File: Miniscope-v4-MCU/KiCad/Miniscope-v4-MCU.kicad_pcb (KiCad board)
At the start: 4 copper layers, 7 x 8 mm, 11 parts, among them J1 Conn_01x14, J2 Conn_01x01, J3 Conn_01x01, J4 Conn_01x01, J5 Conn_01x01, J6 Conn_01x01, J7 Conn_01x01, J8 Conn_01x05, U1 ATmega328-MU

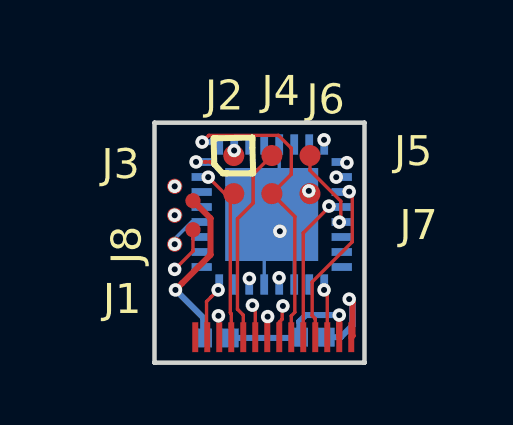
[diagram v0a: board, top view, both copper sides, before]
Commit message: Update MCU PCB with 2x7 grid of FlexPC solder pads
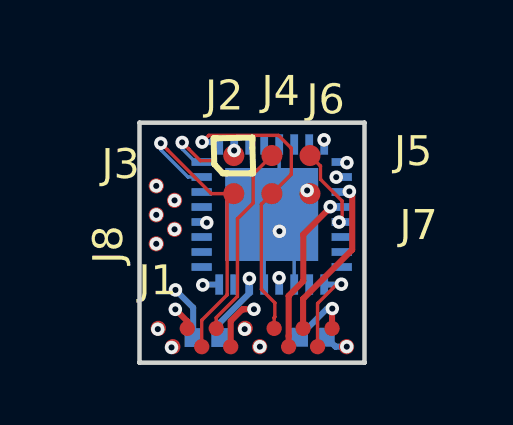
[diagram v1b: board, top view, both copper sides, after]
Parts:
- J1: footprint .Connector:B2B_Flex_14_Single_Row_200x1000_Pad_400P -> .Connector:B2B_Flex_14_Dual_Row_38milx24mil_Pad_20mil
- moved J1 1.27 mm to (50.1, 56.9)
- moved J8 0.61 mm to (50.1, 54.0)
- moved C1 0.34 mm to (51.7, 57.2)
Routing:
- net GND: track 24.3 -> 10.2 mm, vias 4 -> 5
- net +3V3: track 6.00 -> 0.80 mm
- net /MOSI: track 6.33 -> 10.9 mm
- net /MISO: track 8.69 -> 10.4 mm
- net /SCL: track 12.8 -> 11.2 mm
- net /SS_N: track 1.62 -> 3.08 mm
- net /LED: track 1.75 -> 3.07 mm, vias 1 -> 2
- net /MONITOR0: track 7.53 -> 8.39 mm
- net +1V8: track 13.2 -> 12.4 mm
- net /ENT1: track 1.31 -> 1.98 mm, vias 1 -> 2
- net /RESET_N: track 6.19 -> 6.70 mm
- net +5V: vias 0 -> 1
- added copper zone on In4.Cu, net +3V3
- added copper zone on In1.Cu, net GND
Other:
- board size 7 x 8 mm -> 7.5 x 8 mm
- copper layers 4 -> 6

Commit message: Finalize LED-EWL, MCU, and PYTHON480 PCB for fabrication
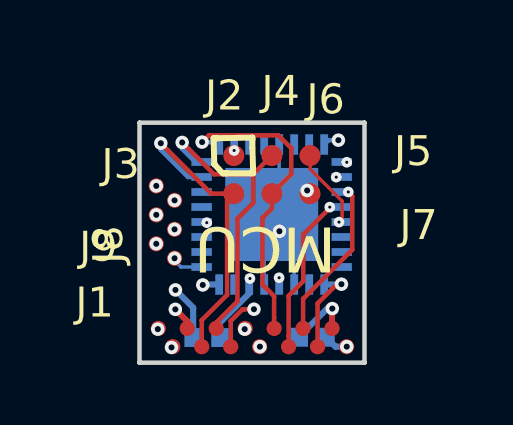
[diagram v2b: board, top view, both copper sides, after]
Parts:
- added J9: Conn_01x01, .Connector:Conn_1x1_700_Circular_Pad, F.Cu at (50.7, 54.5)
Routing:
- net Net-(J9-Pad1): track 0.00 -> 1.03 mm, vias 0 -> 1
- net /MONITOR0: track 8.39 -> 9.32 mm
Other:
- net class Default: via_dia 0.45 -> 0.3556; via_drill 0.2 -> 0.1016
- rule via_min_drill: 0.2 -> 0.1016
- rule via_min_size: 0.45 -> 0.3556
- board text added: "MCU"

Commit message: Add initial folder and files for fabrication array of Miniscope v4 PCBs
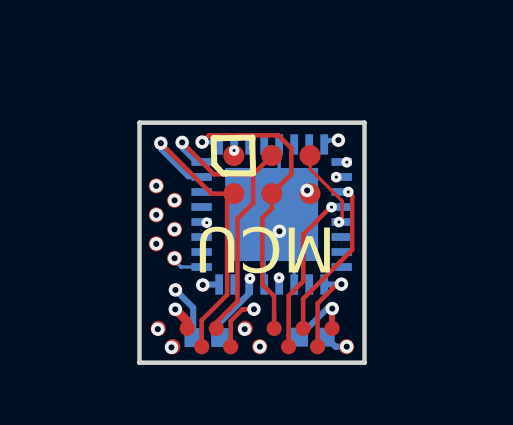
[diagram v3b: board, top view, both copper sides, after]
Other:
- rule pad_to_mask_clearance: 0.051 -> 0.0254
- rule solder_mask_min_width: 0.25 -> 0.1016
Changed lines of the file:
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@@
     (pad_size 0.508 0.508)
     (pad_drill 0)
-    (pad_to_mask_clearance 0.051)
-    (solder_mask_min_width 0.25)
-    (aux_axis_origin 0 0)
+    (pad_to_mask_clearance 0.0254)
+    (solder_mask_min_width 0.1016)
+    (aux_axis_origin 49.5 58)
     (grid_origin 49.5 58)
     (visible_elements 7FFFFFFF)
     (pcbplotparams
       (layerselection 0x010fc_ffffffff)
-      (usegerberextensions false)
+      (usegerberextensions true)
       (usegerberattributes false)
       (usegerberadvancedattributes false)
@@
       (viasonmask false)
       (mode 1)
-      (useauxorigin false)
+      (useauxorigin true)
       (hpglpennumber 1)
       (hpglpenspeed 20)
@@
   (module .Connector:Conn_1x1_700_Circular_Pad (layer F.Cu)
     (at 50.6684 54.5202)
-    (fp_text reference J9 (at -2.54 -0.381) (layer F.SilkS)
+    (fp_text reference J9 (at -2.1684 0.7298) (layer F.SilkS) hide
       (effects (font (size 1 1) (thickness 0.15)))
     )
@@
   (module .Connector:B2B_Flex_14_Dual_Row_38milx24mil_Pad_20mil (layer F.Cu)
     (at 50.127 56.857)
-    (fp_text reference J1 (at -2.127 -0.857) (layer F.SilkS)
+    (fp_text reference J1 (at -1.627 0.393) (layer F.SilkS) hide
       (effects (font (size 1 1) (thickness 0.15)))
     )
@@
   (module .Connector:B2B_Flex_05_Dual_Row_38milx24mil_Pad_20mil (layer F.Cu)
     (at 50.0588 54.0376 90)
-    (fp_text reference J8 (at -0.0254 -1.6002 90) (layer F.SilkS)
+    (fp_text reference J8 (at 0.0376 -1.5588 180) (layer F.SilkS) hide
       (effects (font (size 1 1) (thickness 0.15)))
     )
@@
   (module .Connector:Conn_1x1_700_Circular_Pad (layer F.Cu)
     (at 55.1832 52.3654)
-    (fp_text reference J7 (at 3.6178 1.0508) (layer F.SilkS)
+    (fp_text reference J7 (at 2.8168 0.1346) (layer F.SilkS) hide
       (effects (font (size 1 1) (thickness 0.15)))
     )
@@
   (module .Connector:Conn_1x1_700_Circular_Pad (layer F.Cu)
     (at 55.1832 51.0954)
-    (fp_text reference J6 (at 0.519 -1.8702) (layer F.SilkS)
+    (fp_text reference J6 (at 1.0668 -2.0954) (layer F.SilkS) hide
       (effects (font (size 1 1) (thickness 0.15)))
     )
@@
   (module .Connector:Conn_1x1_700_Circular_Pad (layer F.Cu)
     (at 53.9132 52.3654)
-    (fp_text reference J5 (at 4.71 -1.413) (layer F.SilkS)
+    (fp_text reference J5 (at 4.0868 -1.413) (layer F.SilkS) hide
       (effects (font (size 1 1) (thickness 0.15)))
     )
@@
   (module .Connector:Conn_1x1_700_Circular_Pad (layer F.Cu)
     (at 53.9132 51.0954)
-    (fp_text reference J4 (at 0.2904 -2.1496) (layer F.SilkS)
+    (fp_text reference J4 (at 0.5868 -2.0954) (layer F.SilkS) hide
       (effects (font (size 1 1) (thickness 0.15)))
     )
@@
   (module .Connector:Conn_1x1_700_Circular_Pad (layer F.Cu)
     (at 52.6432 52.3654)
-    (fp_text reference J3 (at -3.7736 -0.9812) (layer F.SilkS)
+    (fp_text reference J3 (at -4.1432 -1.1154) (layer F.SilkS) hide
       (effects (font (size 1 1) (thickness 0.15)))
     )
@@
   (module .Connector:Conn_1x1_700_Circular_Pad (layer F.Cu)
     (at 52.6432 51.0954)
-    (fp_text reference J2 (at -0.3192 -1.9972) (layer F.SilkS)
+    (fp_text reference J2 (at 0.1068 -2.0954) (layer F.SilkS) hide
       (effects (font (size 1 1) (thickness 0.15)))
     )
@@
       (effects (font (size 1.2 1.2) (thickness 0.12)) (justify mirror))
     )
-    (fp_text user %R (at 1.557 4.3688 180) (layer B.SilkS)
+    (fp_text user %R (at 4.4064 5.0606 180) (layer B.SilkS)
       (effects (font (size 2 2) (thickness 0.2)) (justify mirror))
     )
@@
   (via (at 50.0588 52.1072) (size 0.45) (drill 0.2) (layers F.Cu B.Cu) (net 17))
   (via (at 50.6938 56.222) (size 0.45) (drill 0.2) (layers F.Cu B.Cu) (net 17))
-  (segment (start 51.092199 56.620399) (end 50.6938 56.222) (width 0.2032) (layer F.Cu) (net 17))
+  (segment (start 51.092199 56.620399) (end 50.6938 56.222) (width 0.3048) (layer F.Cu) (net 17))
   (segment (start 51.092199 56.857) (end 51.092199 56.620399) (width 0.2032) (layer F.Cu) (net 17))
   (segment (start 52.4764 52.5322) (end 52.6432 52.3654) (width 0.1524) (layer F.Cu) (net 18))
@@
   (segment (start 56.236358 52.815642) (end 56.159497 52.815642) (width 0.1524) (layer B.Cu) (net 24))
   (segment (start 56.159497 52.815642) (end 55.841299 52.815642) (width 0.1524) (layer B.Cu) (net 24))
-  (via (at 55.841299 52.815642) (size 0.3556) (drill 0.1016) (layers F.Cu B.Cu) (net 24))
+  (via (at 55.9008 52.815642) (size 0.3556) (drill 0.1016) (layers F.Cu B.Cu) (net 24))
   (segment (start 56.2414 52.8106) (end 56.236358 52.815642) (width 0.1524) (layer B.Cu) (net 24))
   (via (at 50.0588 53.0724) (size 0.45) (drill 0.2) (layers F.Cu B.Cu) (net 25))
@@
   (segment (start 55.435594 56.026806) (end 56.0786 55.3838) (width 0.1524) (layer F.Cu) (net 26))
   (via (at 50.0588 54.0376) (size 0.45) (drill 0.2) (layers F.Cu B.Cu) (net 27))
-  (segment (start 51.517172 53.55837) (end 51.742171 53.333371) (width 0.2032) (layer In2.Cu) (net 27))
-  (segment (start 51.037942 54.0376) (end 51.517172 53.55837) (width 0.2032) (layer In2.Cu) (net 27))
-  (segment (start 50.0588 54.0376) (end 51.037942 54.0376) (width 0.2032) (layer In2.Cu) (net 27))
+  (segment (start 51.517172 53.55837) (end 51.742171 53.333371) (width 0.1524) (layer In2.Cu) (net 27))
+  (segment (start 51.037942 54.0376) (end 51.517172 53.55837) (width 0.1524) (layer In2.Cu) (net 27))
+  (segment (start 50.0588 54.0376) (end 51.037942 54.0376) (width 0.1524) (layer In2.Cu) (net 27))
   (via (at 51.742171 53.333371) (size 0.3556) (drill 0.1016) (layers F.Cu B.Cu) (net 27))
   (via (at 56.15029 53.3146) (size 0.3556) (drill 0.1016) (layers F.Cu B.Cu) (net 29))
